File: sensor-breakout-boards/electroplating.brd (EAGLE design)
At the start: 24 x 30 mm, 7 parts, among them X1 Type-A Receptacle, X2 2-PIN-CONNECTOR, X3 2-PIN-CONNECTOR, X4 2-PIN-CONNECTOR, X5 2-PIN-CONNECTOR

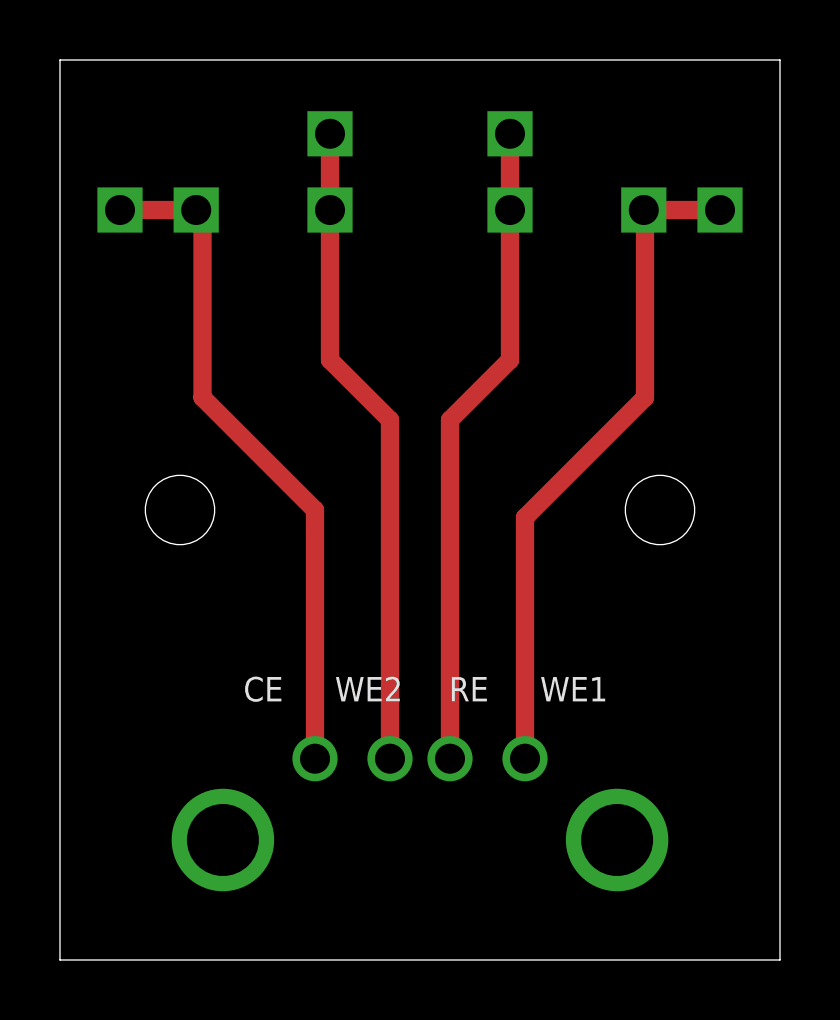
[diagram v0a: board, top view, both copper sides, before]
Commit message: edited electroplating board per Prof. Pap.
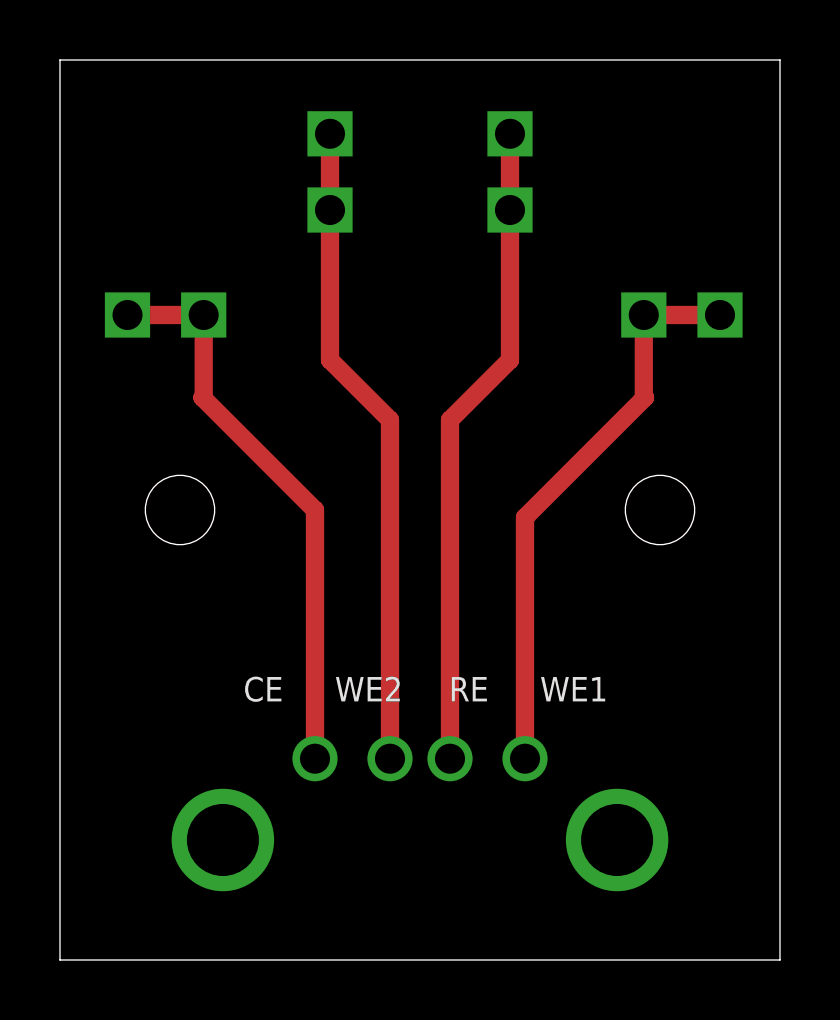
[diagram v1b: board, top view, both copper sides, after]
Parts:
- moved X2 3.51 mm to (2.25, 21.5)
- moved X5 3.50 mm to (22.0, 21.5)
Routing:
- net CE: track 22.5 -> 18.9 mm
- net WE1: track 22.5 -> 19.0 mm
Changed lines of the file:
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@@
 <element name="MOUNTING1" library="sensor-breakout-boards" package="M2-MOUNTING-HOLE" value="M2-MOUNTING-HOLE" x="20" y="15"/>
 <element name="MOUNTING2" library="sensor-breakout-boards" package="M2-MOUNTING-HOLE" value="M2-MOUNTING-HOLE" x="4" y="15"/>
-<element name="X2" library="sensor-breakout-boards" package="2-PIN-HEADER" value="2-PIN-CONNECTOR" x="2" y="25"/>
+<element name="X2" library="sensor-breakout-boards" package="2-PIN-HEADER" value="2-PIN-CONNECTOR" x="2.25" y="21.5"/>
 <element name="X3" library="sensor-breakout-boards" package="2-PIN-HEADER" value="2-PIN-CONNECTOR" x="9" y="25" rot="R90"/>
 <element name="X4" library="sensor-breakout-boards" package="2-PIN-HEADER" value="2-PIN-CONNECTOR" x="15" y="25" rot="R90"/>
-<element name="X5" library="sensor-breakout-boards" package="2-PIN-HEADER" value="2-PIN-CONNECTOR" x="22" y="25" rot="R180"/>
+<element name="X5" library="sensor-breakout-boards" package="2-PIN-HEADER" value="2-PIN-CONNECTOR" x="22" y="21.5" rot="R180"/>
 </elements>
 <signals>
@@
 <contactref element="X2" pad="2"/>
 <contactref element="X2" pad="1"/>
-<wire x1="2" y1="25" x2="4.54" y2="25" width="0.6096" layer="1"/>
 <wire x1="8.5" y1="6.71" x2="8.5" y2="15" width="0.6096" layer="1"/>
 <wire x1="8.5" y1="15" x2="4.75" y2="18.75" width="0.6096" layer="1"/>
-<wire x1="4.75" y1="18.75" x2="4.75" y2="24.79" width="0.6096" layer="1"/>
-<wire x1="4.75" y1="24.79" x2="4.54" y2="25" width="0.6096" layer="1"/>
+<wire x1="4.75" y1="18.75" x2="4.79" y2="18.75" width="0.6096" layer="1"/>
+<wire x1="4.79" y1="18.75" x2="4.79" y2="21.5" width="0.6096" layer="1"/>
+<wire x1="4.79" y1="21.5" x2="2.25" y2="21.5" width="0.6096" layer="1"/>
 </signal>
 <signal name="WE2">
@@
 <wire x1="15.5" y1="6.71" x2="15.5" y2="14.75" width="0.6096" layer="1"/>
 <wire x1="15.5" y1="14.75" x2="19.5" y2="18.75" width="0.6096" layer="1"/>
-<wire x1="19.5" y1="18.75" x2="19.5" y2="24.96" width="0.6096" layer="1"/>
-<wire x1="19.5" y1="24.96" x2="19.46" y2="25" width="0.6096" layer="1"/>
-<wire x1="19.46" y1="25" x2="22" y2="25" width="0.6096" layer="1"/>
+<wire x1="19.5" y1="18.75" x2="19.46" y2="18.75" width="0.6096" layer="1"/>
+<wire x1="19.46" y1="18.75" x2="19.46" y2="21.5" width="0.6096" layer="1"/>
+<wire x1="19.46" y1="21.5" x2="22" y2="21.5" width="0.6096" layer="1"/>
 </signal>
 <signal name="RE">
